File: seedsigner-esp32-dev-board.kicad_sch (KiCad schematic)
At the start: 5 parts, among them J1 Conn_01x05, U1 ESP32-S2-SAOLA-1M, U2 OV_CAMERA, U3 RASPBERRY_PI_3_MODEL_B+

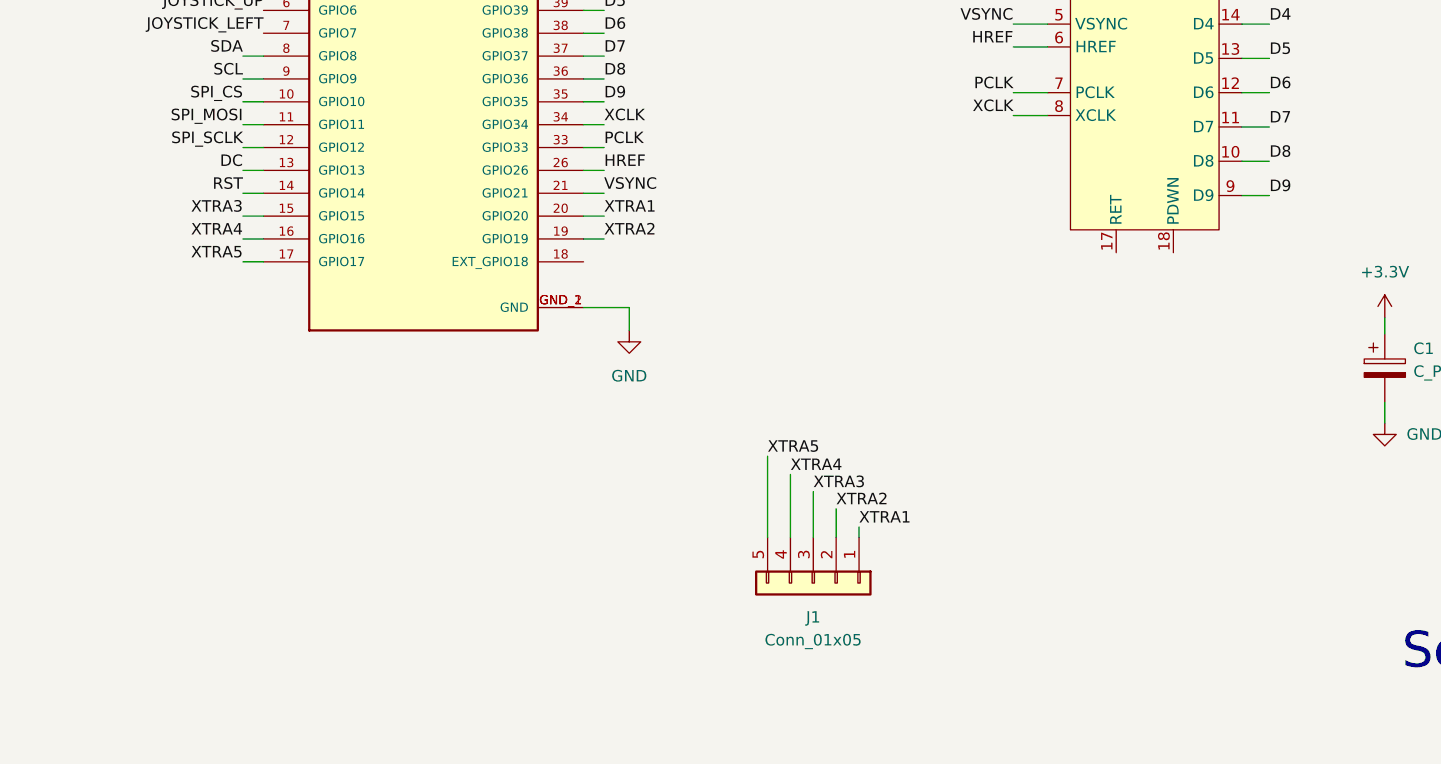
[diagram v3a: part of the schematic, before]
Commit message: add holes and seedsigner logo
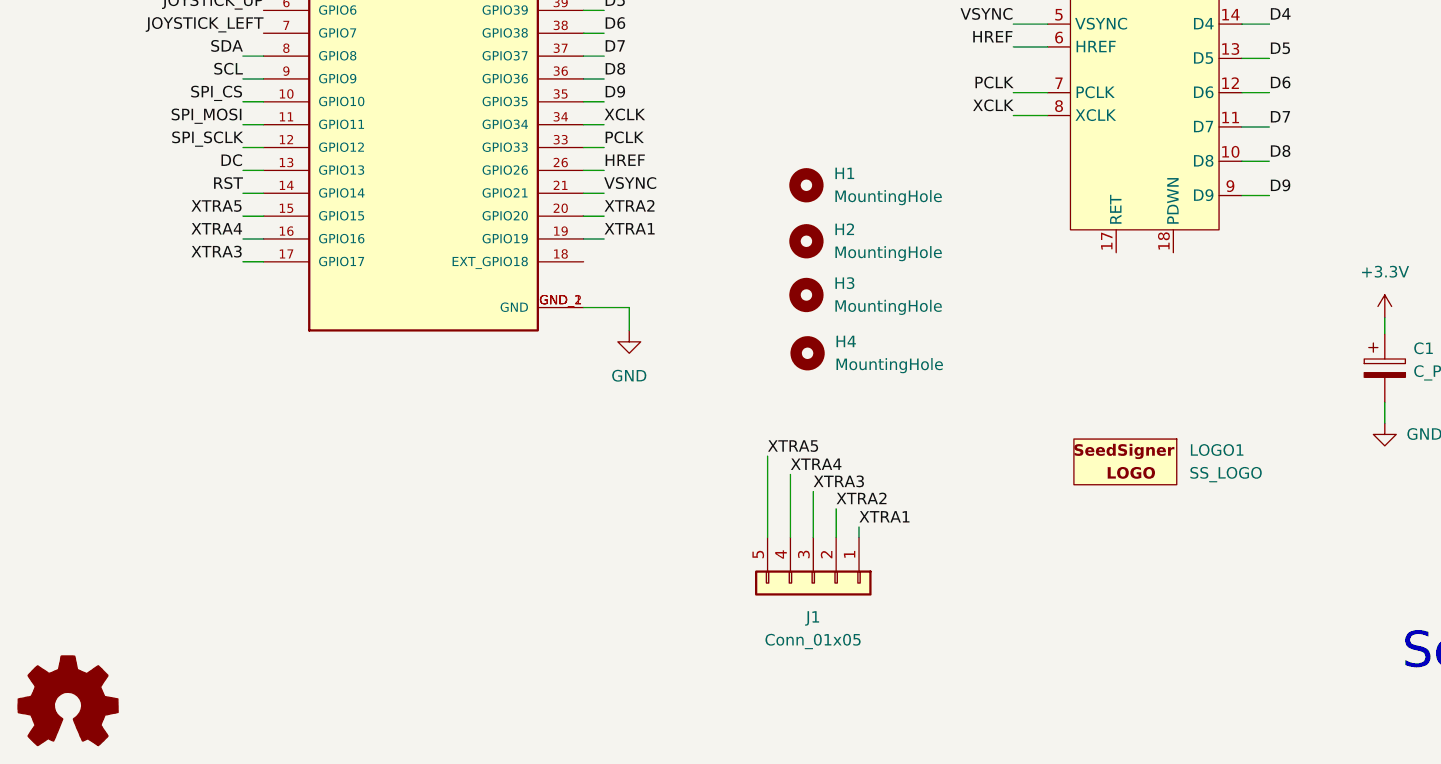
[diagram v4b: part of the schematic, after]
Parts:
- added H1, H2, H3, H4: MountingHole, SeedSigner:MOUNT_HOLE_3MM, symbol Mechanical:MountingHole
- added LOGO1: SS_LOGO, SeedSigner:seedsigner-logo-small, symbol SeedSigner:SS_LOGO
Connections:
- net XTRA1: now also U1.19 (GPIO19); no longer U1.20 (GPIO20)
- net XTRA2: now also U1.20 (GPIO20); no longer U1.19 (GPIO19)
- net XTRA3: now also U1.17 (GPIO17); no longer U1.15 (GPIO15)
- net XTRA5: now also U1.15 (GPIO15); no longer U1.17 (GPIO17)
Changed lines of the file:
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@@
     (effects (font (size 1.27 1.27)) (justify right bottom))
+  )
+  (label "XTRA2" (at 89.916 126.746 0)
+    (effects (font (size 1.27 1.27)) (justify left bottom))
   )
   (label "JOYSTICK_LEFT" (at 52.07 106.426 180)
@@
     (effects (font (size 1.27 1.27)) (justify left bottom))
   )
+  (label "XTRA1" (at 89.916 129.286 0)
+    (effects (font (size 1.27 1.27)) (justify left bottom))
+  )
   (label "DC" (at 193.294 108.204 180)
     (effects (font (size 1.27 1.27)) (justify right bottom))
@@
     (effects (font (size 1.27 1.27)) (justify left bottom))
   )
-  (label "XTRA1" (at 89.916 126.746 0)
-    (effects (font (size 1.27 1.27)) (justify left bottom))
-  )
-  (label "XTRA3" (at 49.784 126.746 180)
+  (label "XTRA3" (at 49.784 131.826 180)
     (effects (font (size 1.27 1.27)) (justify right bottom))
   )
@@
     (effects (font (size 1.27 1.27)) (justify left bottom))
   )
-  (label "XTRA2" (at 89.916 129.286 0)
-    (effects (font (size 1.27 1.27)) (justify left bottom))
-  )
   (label "D9" (at 89.916 114.046 0)
     (effects (font (size 1.27 1.27)) (justify left bottom))
@@
     (effects (font (size 1.27 1.27)) (justify right bottom))
   )
-  (label "XTRA5" (at 49.784 131.826 180)
+  (label "XTRA5" (at 49.784 126.746 180)
     (effects (font (size 1.27 1.27)) (justify right bottom))
   )
@@
     (pin "8")
     (pin "9")
+  )
+  (symbol (lib_id "SeedSigner:SS_LOGO") (at 148.463 152.781 0) (unit 1)
+    (in_bom no) (on_board yes) (fields_autoplaced)
+    (property "Reference" "LOGO1" (id 0) (at 154.94 152.7809 0)
+      (effects (font (size 1.27 1.27)) (justify left))
+    )
+    (property "Value" "SS_LOGO" (id 1) (at 154.94 155.3209 0)
+      (effects (font (size 1.27 1.27)) (justify left))
+    )
+    (property "Footprint" "SeedSigner:seedsigner-logo-small" (id 2) (at 148.463 152.781 0)
+      (effects (font (size 1.27 1.27)) hide)
+    )
+    (property "Datasheet" "" (id 3) (at 148.463 152.781 0)
+      (effects (font (size 1.27 1.27)) hide)
+    )
   )
   (symbol (lib_id "power:+3.3V") (at 252.095 79.756 0) (unit 1)
@@
     (pin "1")
   )
+  (symbol (lib_id "Mechanical:MountingHole") (at 112.395 123.317 0) (unit 1)
+    (in_bom yes) (on_board yes) (fields_autoplaced)
+    (property "Reference" "H1" (id 0) (at 115.443 122.0469 0)
+      (effects (font (size 1.27 1.27)) (justify left))
+    )
+    (property "Value" "MountingHole" (id 1) (at 115.443 124.5869 0)
+      (effects (font (size 1.27 1.27)) (justify left))
+    )
+    (property "Footprint" "SeedSigner:MOUNT_HOLE_3MM" (id 2) (at 112.395 123.317 0)
+      (effects (font (size 1.27 1.27)) hide)
+    )
+    (property "Datasheet" "~" (id 3) (at 112.395 123.317 0)
+      (effects (font (size 1.27 1.27)) hide)
+    )
+  )
   (symbol (lib_id "power:GND") (at 251.714 138.684 0) (unit 1)
     (in_bom yes) (on_board yes) (fields_autoplaced)
@@
     (pin "4")
     (pin "5")
+  )
+  (symbol (lib_id "Mechanical:MountingHole") (at 112.395 129.54 0) (unit 1)
+    (in_bom yes) (on_board yes) (fields_autoplaced)
+    (property "Reference" "H2" (id 0) (at 115.443 128.2699 0)
+      (effects (font (size 1.27 1.27)) (justify left))
+    )
+    (property "Value" "MountingHole" (id 1) (at 115.443 130.8099 0)
+      (effects (font (size 1.27 1.27)) (justify left))
+    )
+    (property "Footprint" "SeedSigner:MOUNT_HOLE_3MM" (id 2) (at 112.395 129.54 0)
+      (effects (font (size 1.27 1.27)) hide)
+    )
+    (property "Datasheet" "~" (id 3) (at 112.395 129.54 0)
+      (effects (font (size 1.27 1.27)) hide)
+    )
+  )
+  (symbol (lib_id "Graphic:Logo_Open_Hardware_Small") (at 30.353 181.229 0) (unit 1)
+    (in_bom yes) (on_board yes) (fields_autoplaced)
+    (property "Reference" "#LOGO1" (id 0) (at 30.353 174.244 0)
+      (effects (font (size 1.27 1.27)) hide)
+    )
+    (property "Value" "Logo_Open_Hardware_Small" (id 1) (at 30.353 186.944 0)
+      (effects (font (size 1.27 1.27)) hide)
+    )
+    (property "Footprint" "" (id 2) (at 30.353 181.229 0)
+      (effects (font (size 1.27 1.27)) hide)
+    )
+    (property "Datasheet" "~" (id 3) (at 30.353 181.229 0)
+      (effects (font (size 1.27 1.27)) hide)
+    )
   )
   (symbol (lib_id "SeedSigner:ESP32-S2-SAOLA-1M") (at 69.85 106.426 0) (unit 1)
@@
     (pin "1")
   )
+  (symbol (lib_id "Mechanical:MountingHole") (at 112.522 141.986 0) (unit 1)
+    (in_bom yes) (on_board yes) (fields_autoplaced)
+    (property "Reference" "H4" (id 0) (at 115.57 140.7159 0)
+      (effects (font (size 1.27 1.27)) (justify left))
+    )
+    (property "Value" "MountingHole" (id 1) (at 115.57 143.2559 0)
+      (effects (font (size 1.27 1.27)) (justify left))
+    )
+    (property "Footprint" "SeedSigner:MOUNT_HOLE_3MM" (id 2) (at 112.522 141.986 0)
+      (effects (font (size 1.27 1.27)) hide)
+    )
+    (property "Datasheet" "~" (id 3) (at 112.522 141.986 0)
+      (effects (font (size 1.27 1.27)) hide)
+    )
+  )
   (symbol (lib_id "power:+3.3V") (at 96.52 70.866 0) (unit 1)
     (in_bom yes) (on_board yes) (fields_autoplaced)
@@
     (pin "1")
   )
+  (symbol (lib_id "Mechanical:MountingHole") (at 112.395 135.509 0) (unit 1)
+    (in_bom yes) (on_board yes) (fields_autoplaced)
+    (property "Reference" "H3" (id 0) (at 115.443 134.2389 0)
+      (effects (font (size 1.27 1.27)) (justify left))
+    )
+    (property "Value" "MountingHole" (id 1) (at 115.443 136.7789 0)
+      (effects (font (size 1.27 1.27)) (justify left))
+    )
+    (property "Footprint" "SeedSigner:MOUNT_HOLE_3MM" (id 2) (at 112.395 135.509 0)
+      (effects (font (size 1.27 1.27)) hide)
+    )
+    (property "Datasheet" "~" (id 3) (at 112.395 135.509 0)
+      (effects (font (size 1.27 1.27)) hide)
+    )
+  )
   (symbol (lib_id "power:GND") (at 92.71 139.446 0) (unit 1)
     (in_bom yes) (on_board yes) (fields_autoplaced)
@@
   )
   (symbol_instances
+    (path "/76ba9397-874a-4123-8f69-af4b62ad31a7"
+      (reference "#LOGO1") (unit 1) (value "Logo_Open_Hardware_Small") (footprint "")
+    )
     (path "/ec888c1c-5fb7-423f-9478-325be56cc580"
       (reference "#PWR01") (unit 1) (value "GND") (footprint "")
@@
       (reference "C1") (unit 1) (value "C_Polarized") (footprint "Capacitor_THT:CP_Radial_D5.0mm_P2.50mm")
     )
+    (path "/3fc227ee-8141-4359-a0d5-a247e1d51fa9"
+      (reference "H1") (unit 1) (value "MountingHole") (footprint "SeedSigner:MOUNT_HOLE_3MM")
+    )
+    (path "/547d787b-b812-4cab-b0d4-b91b301c28ce"
+      (reference "H2") (unit 1) (value "MountingHole") (footprint "SeedSigner:MOUNT_HOLE_3MM")
+    )
+    (path "/e76b018e-a4f4-4184-9d57-2b2ed1c94401"
+      (reference "H3") (unit 1) (value "MountingHole") (footprint "SeedSigner:MOUNT_HOLE_3MM")
+    )
+    (path "/9aeba76a-3ba6-49ef-9c0c-b038b68ee777"
+      (reference "H4") (unit 1) (value "MountingHole") (footprint "SeedSigner:MOUNT_HOLE_3MM")
+    )
     (path "/5193b365-d3e5-416b-aea2-2e44cdead9a6"
       (reference "J1") (unit 1) (value "Conn_01x05") (footprint "Connector_PinHeader_2.54mm:PinHeader_1x05_P2.54mm_Vertical")
     )
+    (path "/2994eabc-87aa-48b5-a9f5-991dfa2701a1"
+      (reference "LOGO1") (unit 1) (value "SS_LOGO") (footprint "SeedSigner:seedsigner-logo-small")
+    )
     (path "/879a1c71-22c7-413f-9f28-8623f77a3636"

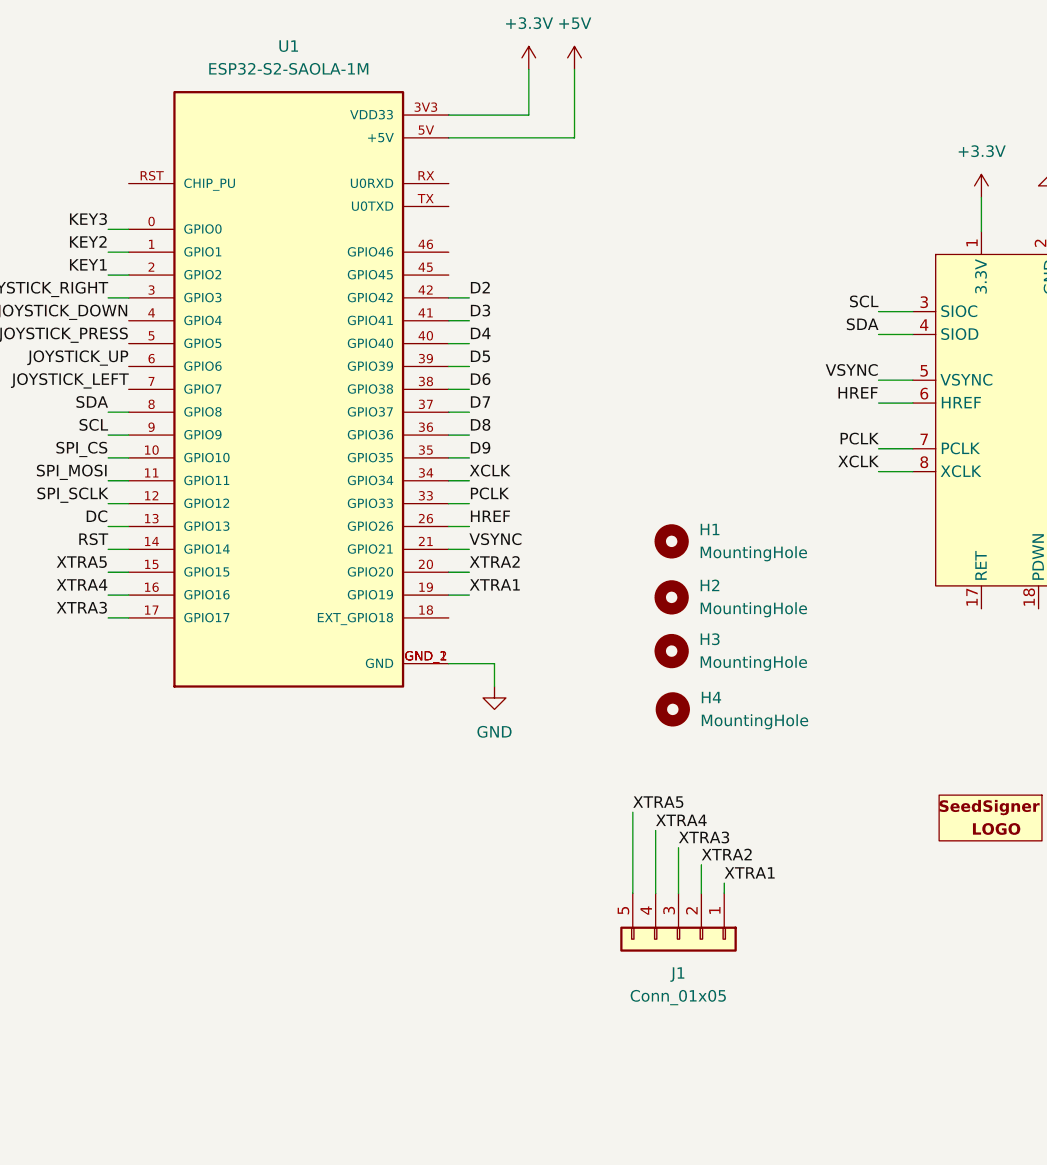
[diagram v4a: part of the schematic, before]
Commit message: cleanup and add header for DE2120
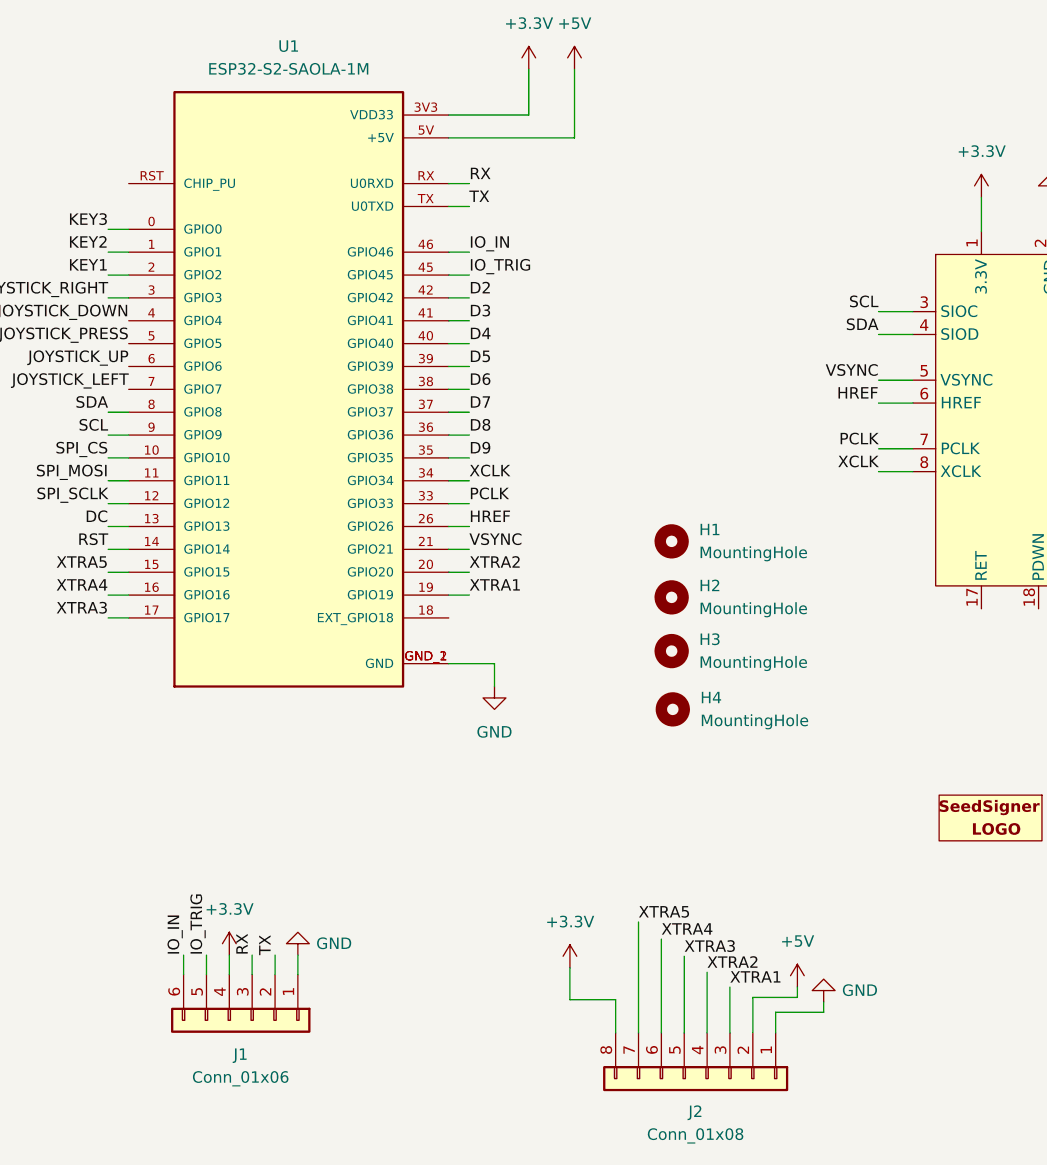
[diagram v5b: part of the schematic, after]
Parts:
- removed J1: Conn_01x05, Connector_PinHeader_2.54mm:PinHeader_1x05_P2.54mm_Vertical, symbol Connector_Generic:Conn_01x05
- added J1: Conn_01x06, Connector_PinHeader_2.54mm:PinHeader_1x06_P2.54mm_Vertical, symbol Connector_Generic:Conn_01x06
- added J2: Conn_01x08, Connector_PinSocket_2.00mm:PinSocket_1x08_P2.00mm_Vertical, symbol Connector_Generic:Conn_01x08
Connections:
- net +3.3V: now also J1.4 (Pin_4), J2.8 (Pin_8)
- net +5V: now also J2.2 (Pin_2)
- net GND: now also J1.1 (Pin_1), J2.1 (Pin_1)
- net XTRA1: now also J2.3 (Pin_3)
- net XTRA2: now also J2.4 (Pin_4)
- net XTRA3: now also J2.5 (Pin_5)
- net XTRA4: now also J2.6 (Pin_6)
- net XTRA5: now also J2.7 (Pin_7)
- net IO_TRIG: now reaches U1.45 (GPIO45)
- net IO_TRIG: now also J1.5 (Pin_5)
- net IO_IN: now reaches U1.46 (GPIO46)
- net IO_IN: now also J1.6 (Pin_6)
- net RX: now reaches U1.RX (U0RXD)
- net RX: now also J1.3 (Pin_3)
- net TX: now reaches U1.TX (U0TXD)
- net TX: now also J1.2 (Pin_2)
